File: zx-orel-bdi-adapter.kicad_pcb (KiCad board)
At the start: 2 copper layers, 100.3 x 80 mm, 22 parts, among them J1 Barrel_Jack_Switch, J2 DB9_Male, SW1 SW_Push_Dual, SW2 SW_DPDT_x2, U1 74LS30, U2 74LS27, U3 74LS04, U4 74LS640, U5 28C256

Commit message: finished orel bdi to zxbus design
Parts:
- removed J-XA1, J-XB1: Conn_01x32_Female, Connector_PinSocket_2.54mm:PinSocket_1x32_P2.54mm_Vertical
- removed J-ZX-BOT1, J-ZX-TOP1: Conn_01x28_Female, Connector_PinSocket_2.54mm:PinSocket_1x28_P2.54mm_Vertical
- removed SW2: SW_DPDT_x2, Button_Switch_THT:SW_NKK_G1xJP
- removed U3: 74LS04, Package_DIP:DIP-14_W7.62mm
- added J3: Conn_02x32_Row_Letter_First, Connector_PinHeader_2.54mm:PinHeader_2x32_P2.54mm_Vertical, B.Cu at (141.0, 52.1)
- added J4: Conn_02x03_Odd_Even, Connector_PinHeader_2.54mm:PinHeader_2x03_P2.54mm_Vertical, F.Cu at (123.8, 47.0)
- added J5: Conn_02x03_Odd_Even, Connector_PinHeader_2.54mm:PinHeader_2x03_P2.54mm_Vertical, F.Cu at (83.8, 47.0)
- added MAP: UA CoA 16x22mm, Symbol:UA CoA 16x22mm Silk, F.Cu at (100.4, 64.6)
- added MAP: UA CoA 21x14mm, Symbol:UA map 21x14mm Silk, F.Cu at (123.8, 74.0)
- added Q1: BC558, Package_TO_SOT_THT:TO-92_Inline_Wide, F.Cu at (82.5, 120.0)
- added Q2: BC558, Package_TO_SOT_THT:TO-92_Inline_Wide, F.Cu at (72.4, 120.0)
- added R3: 680, Resistor_THT:R_Axial_DIN0207_L6.3mm_D2.5mm_P7.62mm_Horizontal, F.Cu at (85.1, 124.5)
- added R4: 2k2, Resistor_THT:R_Axial_DIN0207_L6.3mm_D2.5mm_P7.62mm_Horizontal, F.Cu at (74.9, 127.6)
- added R5: 680, Resistor_THT:R_Axial_DIN0207_L6.3mm_D2.5mm_P7.62mm_Horizontal, F.Cu at (67.3, 124.5)
- added REF**: SolderWire-0.1sqmm_1x02_P3.6mm_D0.4mm_OD1mm, Connector_Wire:SolderWire-0.1sqmm_1x02_P3.6mm_D0.4mm_OD1mm, B.Cu at (141.4, 144.2)
- added REF**: SolderWire-0.1sqmm_1x02_P3.6mm_D0.4mm_OD1mm, Connector_Wire:SolderWire-0.1sqmm_1x02_P3.6mm_D0.4mm_OD1mm, B.Cu at (65.8, 144.2)
- added U6: 74LS32, Package_DIP:DIP-14_W7.62mm, F.Cu at (94.0, 48.3)
- added Z1: ZXBUS, RobikBUS:ZXBUS Slot Connector, F.Cu at (67.9, 146.0)
- added ZXBUSEDGE: ZXBUS Edge Connector, RobikBUS:ZXBUS Edge Connector, B.Cu at (66.7, 162.7)
- R2: value 470 -> 2k2; footprint Resistor_THT:R_Axial_DIN0204_L3.6mm_D1.6mm_P7.62mm_Horizontal -> Resistor_THT:R_Axial_DIN0207_L6.3mm_D2.5mm_P7.62mm_Horizontal
- moved D2 87.8 mm to (131.4, 140.3), turned to 180 degrees
- moved D1 87.6 mm to (143.5, 141.0), turned to -90 degrees
- moved D3 87.3 mm to (139.1, 137.2), turned to 180 degrees
- moved R1 75.8 mm to (127.0, 47.0), turned to 0 degrees
- moved R2 71.2 mm to (77.5, 127.6)
- moved SW1 53.9 mm to (142.3, 40.5), turned to -90 degrees
- moved C1 50.5 mm to (132.7, 52.1), turned to -90 degrees
- moved J2 47.6 mm to (70.2, 58.9), turned to -90 degrees
- moved U2 40.9 mm to (87.0, 101.6), turned to 180 degrees
- moved RN1 36.7 mm to (75.4, 74.9), turned to 90 degrees
- moved C3 31.4 mm to (81.9, 81.9), turned to 0 degrees
- moved U4 22.7 mm to (87.0, 77.5), turned to 180 degrees
- moved U1 22.2 mm to (74.3, 101.6), turned to 180 degrees
- moved C2 20.0 mm to (66.7, 82.5), turned to 0 degrees
- moved U5 15.5 mm to (94.0, 67.3)
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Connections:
- R2 pad 1: Net-(R2-Pad1) -> Net-(U5-~{CS})
- R2 pad 2: //EXT_ROMCS -> Net-(Q1-B)
- U2 pad 10: /A14 -> unconnected-(U2-Pad10)
- U2 pad 11: //MREQ -> unconnected-(U2-Pad11)
- U2 pad 8: Net-(U2-Pad8) -> unconnected-(U2-Pad8)
- U2 pad 9: /A15 -> unconnected-(U2-Pad9)
- U5 pad 1: //BETA -> /TRDOS ROM ONLY
- U5 pad 20: //EXT_ROMCS -> Net-(U5-~{CS})
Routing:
- net (no net): track 0.00 -> 470.5 mm
- net +5V: track 153.7 -> 451.9 mm, vias 0 -> 1
- net /TRDOS ROM ONLY: track 0.00 -> 241.6 mm, vias 0 -> 3
- net GND: track 288.2 -> 503.5 mm, vias 0 -> 4
- net Net-(D1-A): track 0.00 -> 197.3 mm
- net /A11: track 0.00 -> 194.5 mm, vias 0 -> 5
- net /A10: track 0.00 -> 188.6 mm, vias 0 -> 5
- net /A14: track 0.00 -> 183.5 mm, vias 0 -> 5
- net /A15: track 0.00 -> 175.4 mm, vias 0 -> 3
- net /A13: track 0.00 -> 169.4 mm, vias 0 -> 5
- net //IORQ: track 0.00 -> 164.8 mm, vias 0 -> 5
- net /A07: track 21.5 -> 184.1 mm, vias 0 -> 7
- net /A09: track 0.00 -> 160.7 mm, vias 0 -> 5
- net /A04: track 54.7 -> 212.4 mm, vias 2 -> 5
- net //RD: track 30.4 -> 187.7 mm, vias 0 -> 6
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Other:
- board size 100.3 x 80 mm -> 83.8 x 129.7 mm
- board text added: "AUTO"
- board text added: "Designed by Maksym / 7FFD"
- board text added: "KJOY"
- board text added: "OFF"
- board text added: "ON"
- board text added: "ROM"
- board text added: "TRD ONLY"
- board text added: "TRD+B48"
- board text added: "http://7ffd.geektimes.eu/"

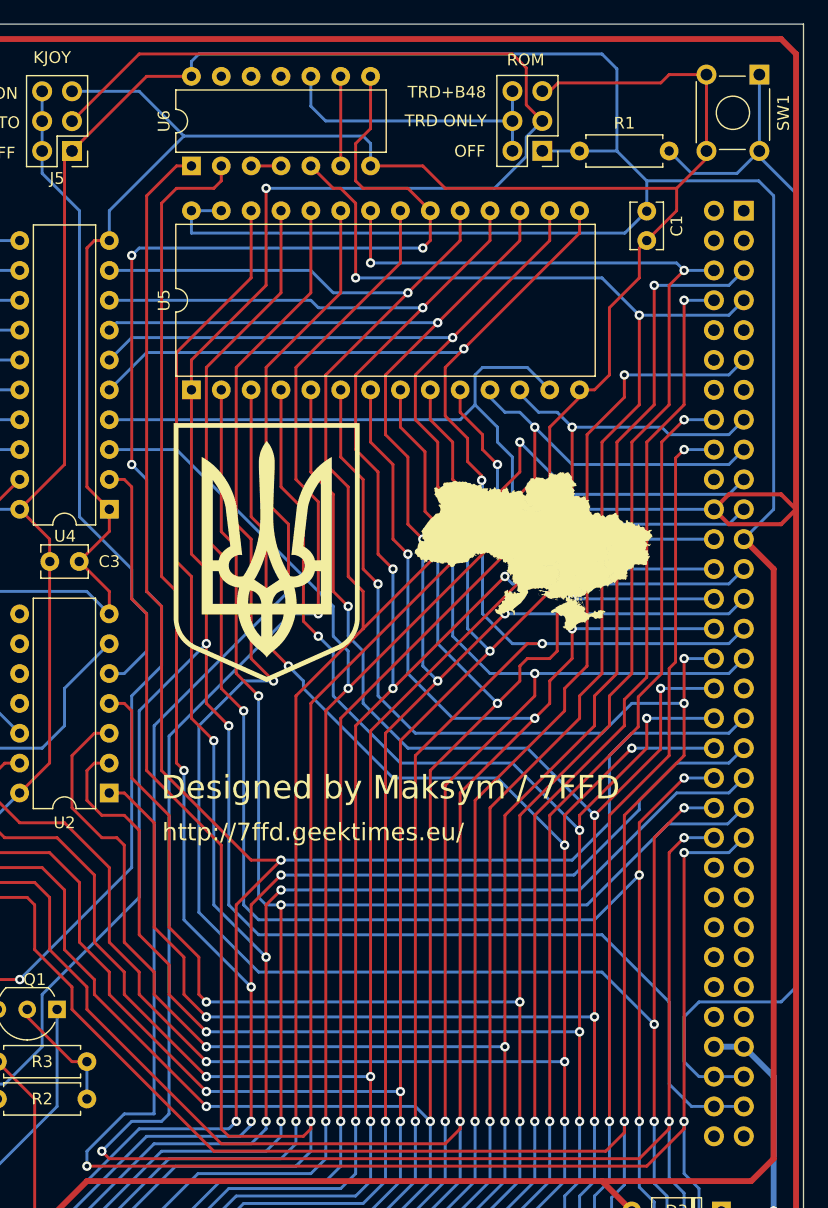
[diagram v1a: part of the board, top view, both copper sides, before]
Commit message: fixed BETA and /BETA output usage to block TRDOS only and re-routed pcb
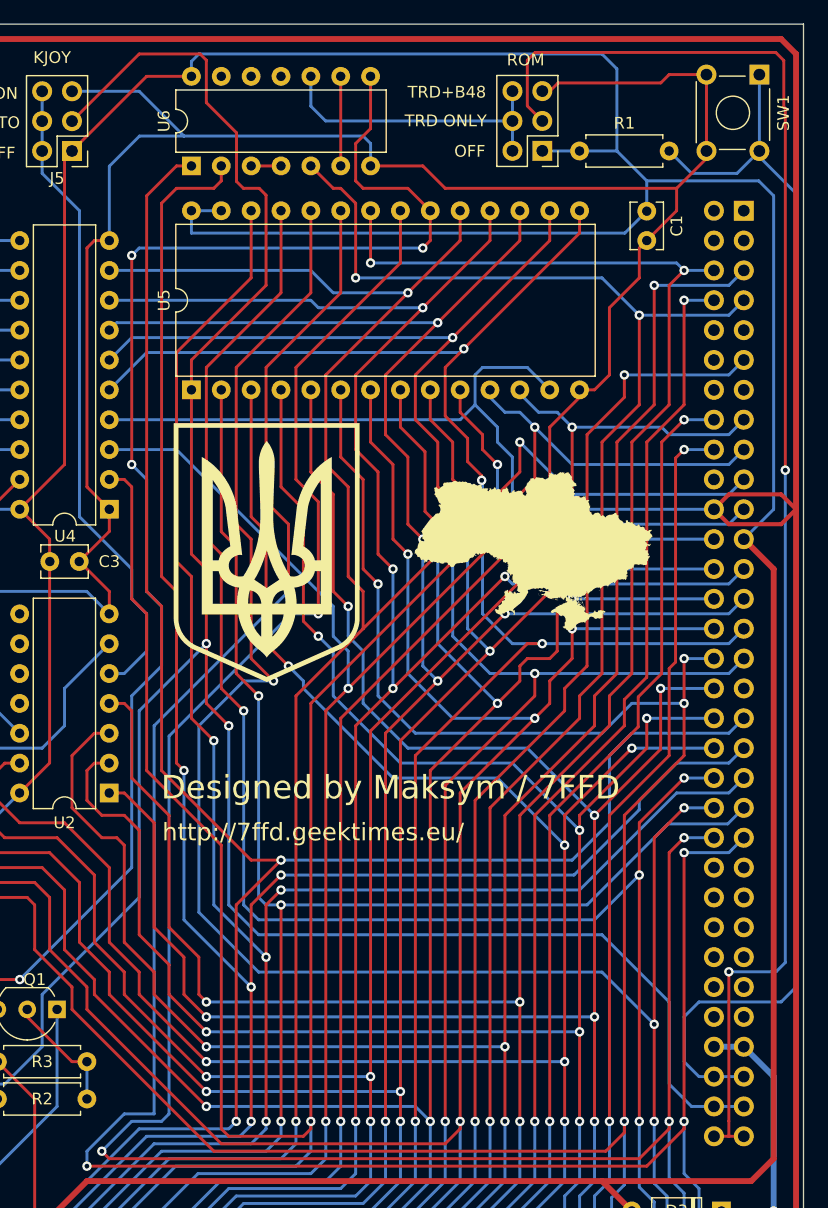
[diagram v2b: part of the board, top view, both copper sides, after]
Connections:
- J3 pad 61: /TRDOS ROM ONLY -> //BETA
- J3 pad 62: /TRDOS ROM ONLY -> //BETA
- J3 pad 63: unconnected-(J3-Pin_63-Pad63) -> /BETA
- J3 pad 64: unconnected-(J3-Pin_64-Pad64) -> /BETA
- J4 pad 3: /TRDOS ROM ONLY -> /BETA
- J5 pad 3: /TRDOS ROM ONLY -> //BETA
- R4 pad 1: /TRDOS ROM ONLY -> //BETA
- U5 pad 1: /TRDOS ROM ONLY -> //BETA
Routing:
- net /TRDOS ROM ONLY: track 241.6 -> 0.00 mm, vias 3 -> 0
- net //BETA: track 0.00 -> 196.0 mm, vias 0 -> 2
- net /BETA: track 0.00 -> 126.6 mm, vias 0 -> 2
- net GND: track 503.5 -> 505.7 mm

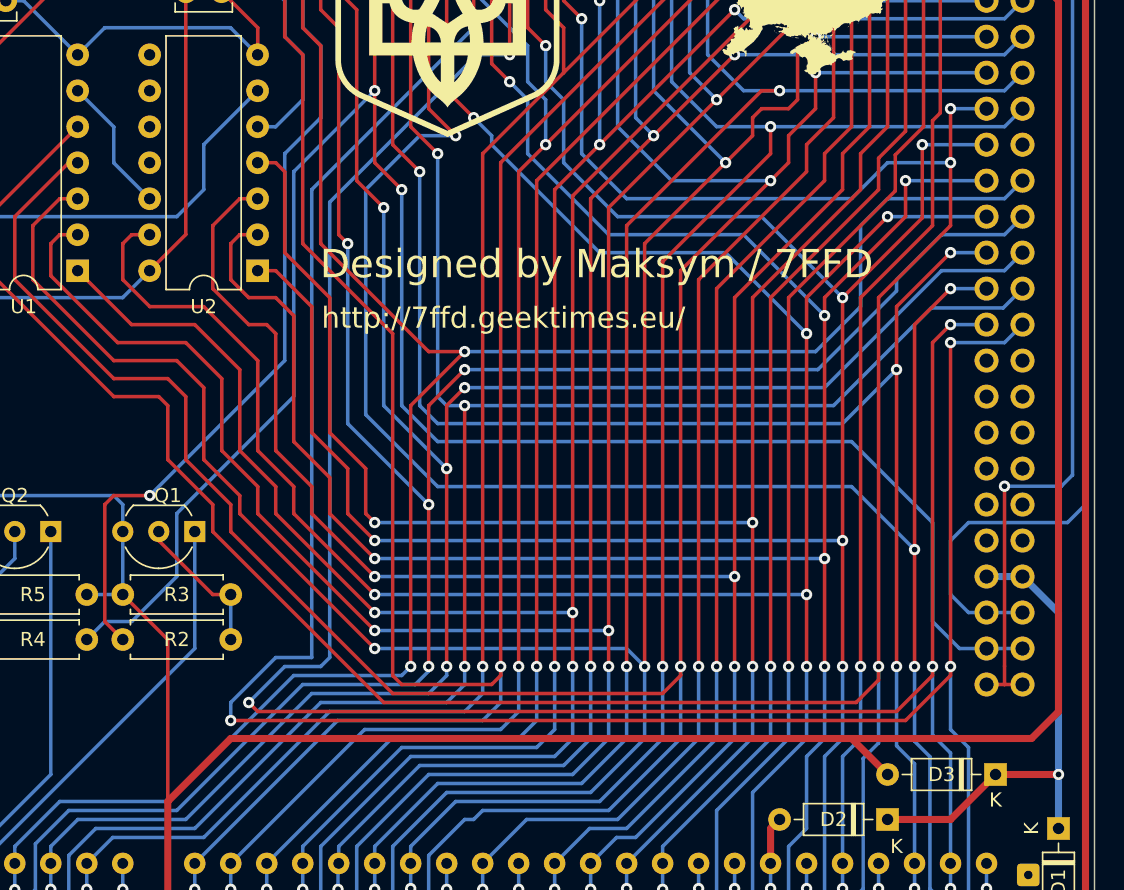
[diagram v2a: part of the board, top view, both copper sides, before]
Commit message: Fixed bug with flipped TRDOS signal
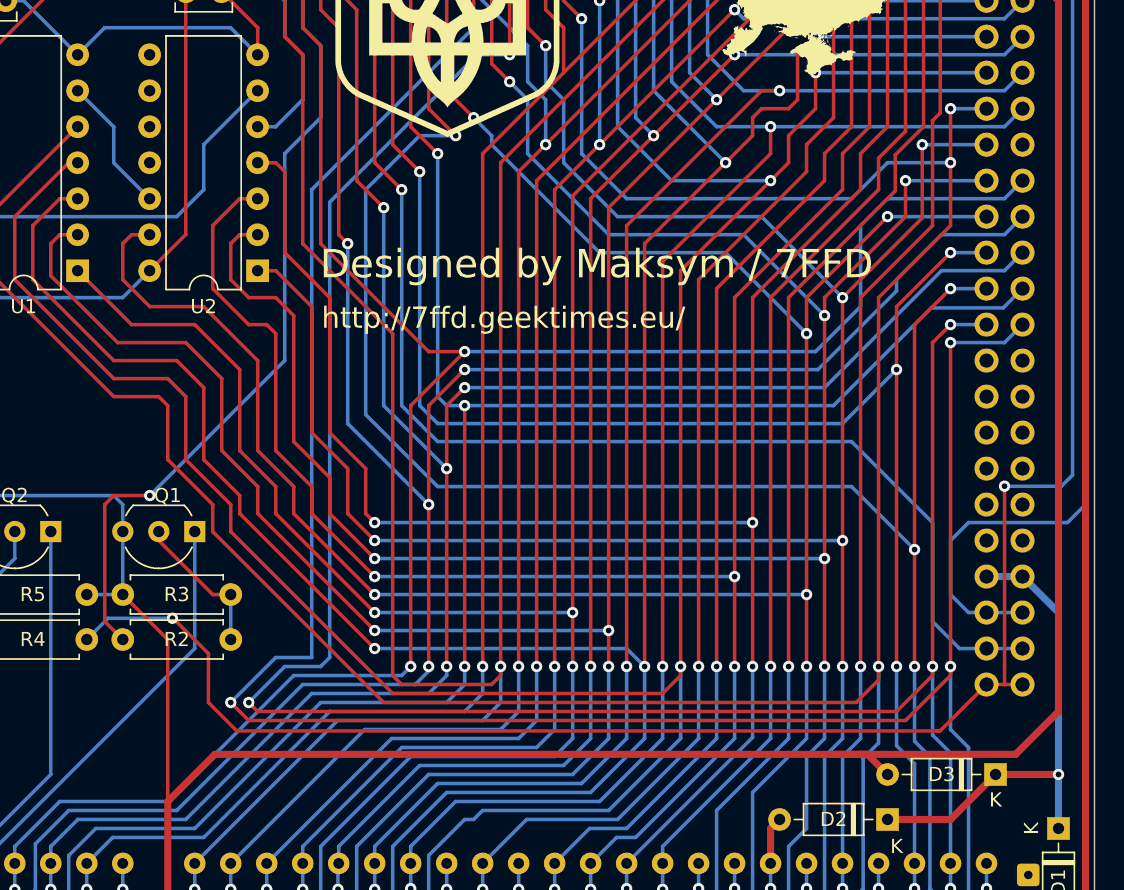
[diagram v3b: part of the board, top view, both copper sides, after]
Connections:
- R4 pad 1: //BETA -> /BETA
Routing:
- net /BETA: track 126.6 -> 197.4 mm, vias 2 -> 3
- net //BETA: track 196.0 -> 147.7 mm, vias 2 -> 1
- net /A11: track 194.5 -> 193.7 mm
- net +5V: track 451.9 -> 452.6 mm
